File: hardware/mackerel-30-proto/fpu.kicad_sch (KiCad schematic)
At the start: 11 parts, among them U11 MC68882

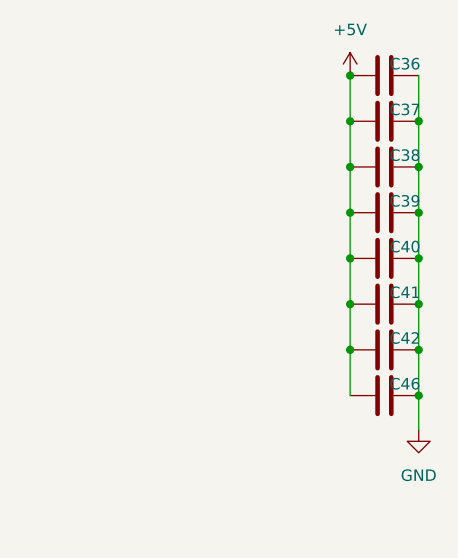
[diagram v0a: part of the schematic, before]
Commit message: Mack-30 routed except for expansion header
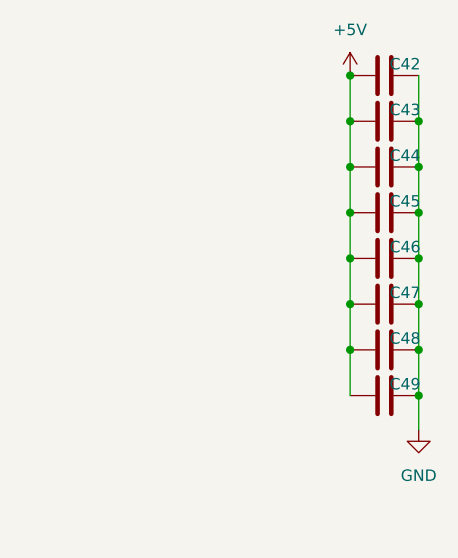
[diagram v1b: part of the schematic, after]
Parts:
- renumbered C36 to C42, C37 to C43, C38 to C44, C39 to C45, C40 to C46, C41 to C47, C42 to C48, C46 to C49
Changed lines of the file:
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@@
 		(dnp no)
 		(fields_autoplaced yes)
-		(property "Reference" "#PWR070"
+		(property "Reference" "#PWR078"
 			(at 57.15 50.8 0)
 			(effects
@@
 			(project ""
 				(path "/9307474f-ec99-494d-b4c9-fbd0b10ce86a/a9f13681-faa6-4706-8ec9-421e908e3ee4"
-					(reference "#PWR070")
+					(reference "#PWR078")
 					(unit 1)
 				)
@@
 		(on_board yes)
 		(dnp no)
-		(property "Reference" "C37"
+		(property "Reference" "C43"
 			(at 185.166 39.37 90)
 			(effects
@@
 			(project "mackerel-30-proto"
 				(path "/9307474f-ec99-494d-b4c9-fbd0b10ce86a/a9f13681-faa6-4706-8ec9-421e908e3ee4"
-					(reference "C37")
+					(reference "C43")
 					(unit 1)
 				)
@@
 		(dnp no)
 		(fields_autoplaced yes)
-		(property "Reference" "#PWR073"
+		(property "Reference" "#PWR081"
 			(at 179.07 39.37 0)
 			(effects
@@
 			(project "mackerel-30-proto"
 				(path "/9307474f-ec99-494d-b4c9-fbd0b10ce86a/a9f13681-faa6-4706-8ec9-421e908e3ee4"
-					(reference "#PWR073")
+					(reference "#PWR081")
 					(unit 1)
 				)
@@
 		(dnp no)
 		(fields_autoplaced yes)
-		(property "Reference" "#PWR072"
+		(property "Reference" "#PWR080"
 			(at 107.95 147.32 0)
 			(effects
@@
 			(project ""
 				(path "/9307474f-ec99-494d-b4c9-fbd0b10ce86a/a9f13681-faa6-4706-8ec9-421e908e3ee4"
-					(reference "#PWR072")
+					(reference "#PWR080")
 					(unit 1)
 				)
@@
 		(dnp no)
 		(fields_autoplaced yes)
-		(property "Reference" "#PWR071"
+		(property "Reference" "#PWR079"
 			(at 85.09 52.07 0)
 			(effects
@@
 			(project ""
 				(path "/9307474f-ec99-494d-b4c9-fbd0b10ce86a/a9f13681-faa6-4706-8ec9-421e908e3ee4"
-					(reference "#PWR071")
+					(reference "#PWR079")
 					(unit 1)
 				)
@@
 		(on_board yes)
 		(dnp no)
-		(property "Reference" "C40"
+		(property "Reference" "C46"
 			(at 185.166 54.61 90)
 			(effects
@@
 			(project "mackerel-30-proto"
 				(path "/9307474f-ec99-494d-b4c9-fbd0b10ce86a/a9f13681-faa6-4706-8ec9-421e908e3ee4"
-					(reference "C40")
+					(reference "C46")
 					(unit 1)
 				)
@@
 		(dnp no)
 		(fields_autoplaced yes)
-		(property "Reference" "#PWR074"
+		(property "Reference" "#PWR082"
 			(at 186.69 81.28 0)
 			(effects
@@
 			(project ""
 				(path "/9307474f-ec99-494d-b4c9-fbd0b10ce86a/a9f13681-faa6-4706-8ec9-421e908e3ee4"
-					(reference "#PWR074")
+					(reference "#PWR082")
 					(unit 1)
 				)
@@
 		(on_board yes)
 		(dnp no)
-		(property "Reference" "C41"
+		(property "Reference" "C47"
 			(at 185.166 59.69 90)
 			(effects
@@
 			(project "mackerel-30-proto"
 				(path "/9307474f-ec99-494d-b4c9-fbd0b10ce86a/a9f13681-faa6-4706-8ec9-421e908e3ee4"
-					(reference "C41")
+					(reference "C47")
 					(unit 1)
 				)
@@
 		(on_board yes)
 		(dnp no)
-		(property "Reference" "C38"
+		(property "Reference" "C44"
 			(at 185.166 44.45 90)
 			(effects
@@
 			(project "mackerel-30-proto"
 				(path "/9307474f-ec99-494d-b4c9-fbd0b10ce86a/a9f13681-faa6-4706-8ec9-421e908e3ee4"
-					(reference "C38")
+					(reference "C44")
 					(unit 1)
 				)
@@
 		(on_board yes)
 		(dnp no)
-		(property "Reference" "C36"
+		(property "Reference" "C42"
 			(at 185.166 34.29 90)
 			(effects
@@
 			(project "mackerel-30-proto"
 				(path "/9307474f-ec99-494d-b4c9-fbd0b10ce86a/a9f13681-faa6-4706-8ec9-421e908e3ee4"
-					(reference "C36")
+					(reference "C42")
 					(unit 1)
 				)
@@
 		(on_board yes)
 		(dnp no)
-		(property "Reference" "C39"
+		(property "Reference" "C45"
 			(at 185.166 49.53 90)
 			(effects
@@
 			(project "mackerel-30-proto"
 				(path "/9307474f-ec99-494d-b4c9-fbd0b10ce86a/a9f13681-faa6-4706-8ec9-421e908e3ee4"
-					(reference "C39")
+					(reference "C45")
 					(unit 1)
 				)
@@
 		(on_board yes)
 		(dnp no)
-		(property "Reference" "C42"
+		(property "Reference" "C48"
 			(at 185.166 64.77 90)
 			(effects
@@
 			(project "mackerel-30-proto"
 				(path "/9307474f-ec99-494d-b4c9-fbd0b10ce86a/a9f13681-faa6-4706-8ec9-421e908e3ee4"
-					(reference "C42")
+					(reference "C48")
 					(unit 1)
 				)
@@
 		(on_board yes)
 		(dnp no)
-		(property "Reference" "C46"
+		(property "Reference" "C49"
 			(at 185.166 69.85 90)
 			(effects
@@
 			(project "mackerel-30-proto"
 				(path "/9307474f-ec99-494d-b4c9-fbd0b10ce86a/a9f13681-faa6-4706-8ec9-421e908e3ee4"
-					(reference "C46")
-					(unit 1)
-				)
+					(reference "C49")
+					(unit 1)
+				)

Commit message: PCB cleanup
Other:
- title: Mackerel-30 Proto -> Mackerel-30
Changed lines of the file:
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@@
 	(paper "A")
 	(title_block
-		(title "Mackerel-30 Proto")
-		(date "2024-10-05")
-		(rev "1.0")
+		(title "Mackerel-30")
+		(date "2024-11-09")
+		(rev "0.1")
 		(company "Colin Maykish")
 	)
